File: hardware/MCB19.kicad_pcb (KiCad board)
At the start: 2 copper layers, 172.8 x 81.5 mm, 137 parts, among them J401 USART, J402 DISABLE, J601 RJ45, J602 RJ45, J611 +BAT_IN, J612 -BAT_IN, J613 +BAT_OUT, J614 -BAT_OUT, K601 G5LE-1, Q601 IRFP260N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

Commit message: Mudança na leitura de Vin
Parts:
- C619: footprint Capacitor_SMD:C_0805_2012Metric_Pad1.15x1.40mm_HandSolder -> Capacitor_SMD:C_0805_2012Metric_Pad1.18x1.45mm_HandSolder
- J402: value DISABLE -> Conn_01x02_Socket
- R609: value 15k -> 20k; footprint Resistor_SMD:R_0805_2012Metric_Pad1.15x1.40mm_HandSolder -> Capacitor_SMD:C_0805_2012Metric_Pad1.18x1.45mm_HandSolder; moved to F.Cu
- R610: value 1k2 -> 5k6; footprint Resistor_SMD:R_0805_2012Metric_Pad1.15x1.40mm_HandSolder -> MCB19:R_0805_2012Metric_Pad1.15x1.40mm_HandSolder; moved to F.Cu
- U401: value ATMEGA328P-PU -> ATmega328-P; footprint Package_DIP:DIP-28_W7.62mm_Socket -> Package_DIP:DIP-28_W7.62mm_LongPads
- moved R610 38.8 mm to (72.7, 118.1), turned to 0 degrees
- moved R609 35.5 mm to (72.7, 115.9)
- moved J402 2.45 mm to (167.9, 90.4), turned to 180 degrees
- moved L601 1.19 mm to (137.8, 89.9)
- moved C504 0.32 mm to (171.0, 66.5)
- moved C301 0.27 mm to (208.5, 62.0)
- moved C501 0.27 mm to (175.0, 61.5)
- moved C304 0.18 mm to (204.5, 67.0)
- moved U401 0.13 mm to (158.6, 121.0)
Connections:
- net /CANBUS/CS renamed /MCU/MCP_SS
- net /CANBUS/INT renamed /MCU/MCP_INT
- net /driver/LM324A renamed /MCU/LM324_A
- net /driver/LM324B renamed /MCU/LM324_B
- J402 pad 1: GND -> Net-(J402-Pin_1)
- J402 pad 2: Net-(J402-Pad2) -> GND
- R410 pad 1: Net-(J402-Pad2) -> Net-(J402-Pin_1)
- R609 pad 2: Net-(C603-Pad1) -> Net-(F602-Pad1)
- U201 pad 5: (no net) -> unconnected-(U201-SPLIT-Pad5)
- U202 pad 10: (no net) -> unconnected-(U202-~{RX1BF}-Pad10)
- U202 pad 11: (no net) -> unconnected-(U202-~{RX0BF}-Pad11)
- U202 pad 3: (no net) -> unconnected-(U202-CLKOUT/SOF-Pad3)
- U202 pad 4: (no net) -> unconnected-(U202-~{TX0RTS}-Pad4)
- U202 pad 5: (no net) -> unconnected-(U202-~{TX1RTS}-Pad5)
- U202 pad 6: (no net) -> unconnected-(U202-~{TX2RTS}-Pad6)
- U401 pad 11: Net-(J402-Pad2) -> Net-(J402-Pin_1)
- U401 pad 12: (no net) -> unconnected-(U401-PD6-Pad12)
- U401 pad 26: (no net) -> unconnected-(U401-PC3-Pad26)
- U401 pad 27: (no net) -> unconnected-(U401-PC4-Pad27)
- U401 pad 28: (no net) -> unconnected-(U401-PC5-Pad28)
- U401 pad 5: (no net) -> unconnected-(U401-PD3-Pad5)
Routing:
- net Net-(U603A-+): track 43.6 -> 83.1 mm, vias 0 -> 1
- net GND: track 856.1 -> 876.2 mm
- net +5V: track 263.3 -> 283.2 mm
- net Net-(J402-Pin_1): track 0.00 -> 19.0 mm
- net Net-(J402-Pad2): track 17.7 -> 0.00 mm
- net Net-(U602--): track 62.7 -> 69.4 mm
- net Net-(D501-K): track 50.1 -> 56.8 mm
- net Net-(U401-PC2): track 5.73 -> 11.5 mm
- net Net-(U401-PC1): track 5.75 -> 11.4 mm
- net Net-(U401-PC0): track 5.63 -> 11.3 mm
- net /MISO: track 77.0 -> 82.6 mm
- net +12V: track 136.5 -> 141.6 mm
- net Net-(U401-PD4): track 4.67 -> 9.31 mm
- net Net-(F602-Pad1): track 247.5 -> 252.0 mm
- net /MCU/USART_TX: track 8.22 -> 12.4 mm
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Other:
- net class Default removed
- net class Shunt removed
- net class power removed

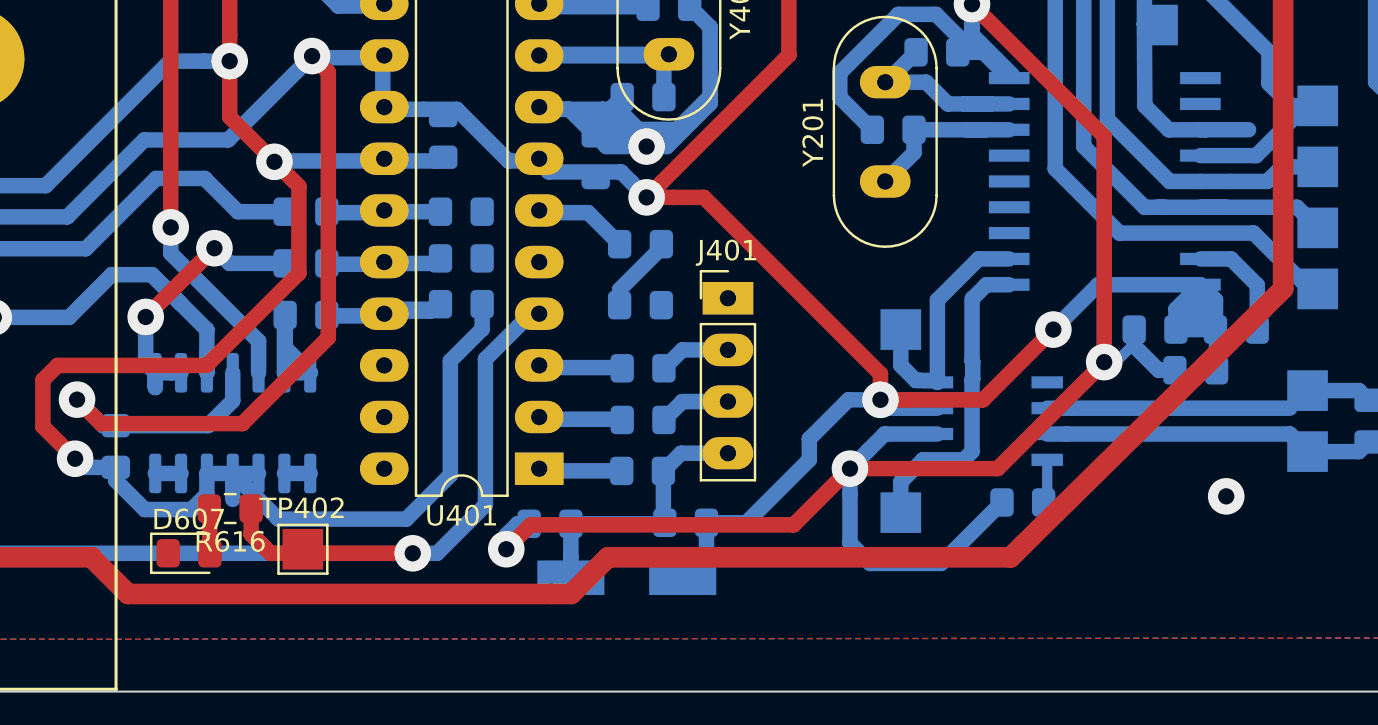
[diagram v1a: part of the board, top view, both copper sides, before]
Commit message: Schematic organization improvement, use <driver> sheet as example
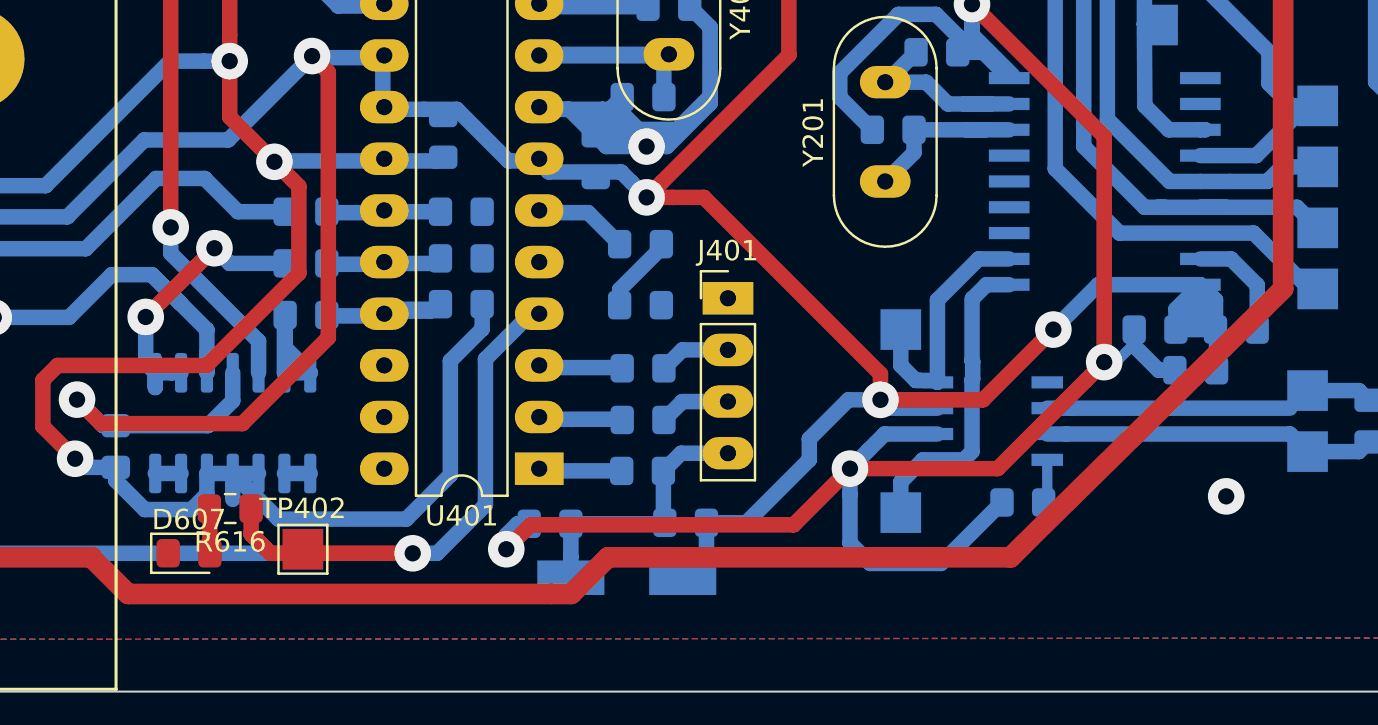
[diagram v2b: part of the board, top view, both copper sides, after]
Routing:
- net /MCU/MCP_INT: track 64.7 -> 62.6 mm
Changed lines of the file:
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@@
 			(psa4output no)
 			(plot_black_and_white yes)
+			(plotinvisibletext no)
 			(sketchpadsonfab no)
 			(plotpadnumbers no)
@@
 	)
 	(segment
-		(start 138.513469 127.286531)
-		(end 138.486531 127.286531)
-		(width 0.762)
-		(layer "F.Cu")
-		(net 49)
-	)
-	(segment
 		(start 159.2 127.2)
 		(end 138.4 127.2)
@@
 		(width 0.762)
 		(layer "B.Cu")
-		(net 64)
-	)
-	(segment
-		(start 191.377 104.375)
-		(end 193.5 104.375)
-		(width 0.762)
-		(layer "B.Cu")

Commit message: Atualiza layout PCB e arquivos de produção
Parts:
- added D1: Zener 5V1, Diode_SMD:D_MiniMELF, F.Cu at (137.0, 105.5)
- added D2: Zener 5V1, Diode_SMD:D_MiniMELF, F.Cu at (131.4, 120.6)
- added D3: ESD5Zxx, Diode_SMD:D_SOD-523, F.Cu at (148.0, 108.5)
- added D4: BAT54J, Diode_SMD:D_SOD-323F, F.Cu at (137.9, 103.0)
- added D5: BAT54J, Diode_SMD:D_SOD-323F, F.Cu at (128.8, 119.6)
- added D6: ESD5Zxx, Diode_SMD:D_SOD-523, F.Cu at (148.0, 111.0)
- added D7: ESD5Zxx, Diode_SMD:D_SOD-523, F.Cu at (148.0, 113.5)
- R407, R408, R409: value 680 -> 10k
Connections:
- net Net-(D602-A) renamed /driver/GATE_LS
- net Net-(D603-A) renamed /driver/GATE_HS
- net Net-(D605-A) renamed /driver/HIGH_SOURCE
- net Net-(U602--) renamed /driver/Shunt-
- C613 pad 1: +BATT -> GND
- C614 pad 1: +BATT -> GND
- C615 pad 1: +BATT -> GND
- C616 pad 1: +BATT -> GND
- C622 pad 1: +BATT -> GND
- C623 pad 1: +BATT -> GND
- C624 pad 1: +BATT -> GND
- C625 pad 1: +BATT -> GND
- C626 pad 1: +BATT -> GND
- C627 pad 1: +BATT -> GND
- D604 pad 2: +BATT -> GND
- F601 pad 1: +BATT -> GND
- F602 pad 1: Net-(F602-Pad1) -> /driver/bat_out_+
- K601 pad 3: Net-(F602-Pad1) -> /driver/bat_out_+
- Q601 pad 2: +BATT -> GND
- R607 pad 2: +BATT -> GND
- R609 pad 2: Net-(F602-Pad1) -> /driver/bat_out+
- R613 pad 2: +BATT -> GND
- R614 pad 1: GND -> /driver/bat_in_-
- R615 pad 2: +BATT -> GND
- R618 pad 1: Net-(F602-Pad1) -> /driver/bat_out_+
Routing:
- net Net-(F602-Pad1): track 252.0 -> 0.00 mm, vias 1 -> 0
- net (no net): track 0.00 -> 252.0 mm, vias 0 -> 1
- net Net-(D2-K): track 83.1 -> 89.0 mm
- net GND: track 876.2 -> 880.9 mm
- net +5V: track 283.2 -> 278.7 mm
- net Net-(D1-K): track 66.6 -> 69.9 mm
- net Net-(D3-K): track 11.3 -> 13.6 mm
- net Net-(D6-K): track 11.4 -> 13.8 mm
- net Net-(D7-K): track 11.5 -> 13.9 mm
